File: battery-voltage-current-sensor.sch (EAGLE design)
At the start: 1 part

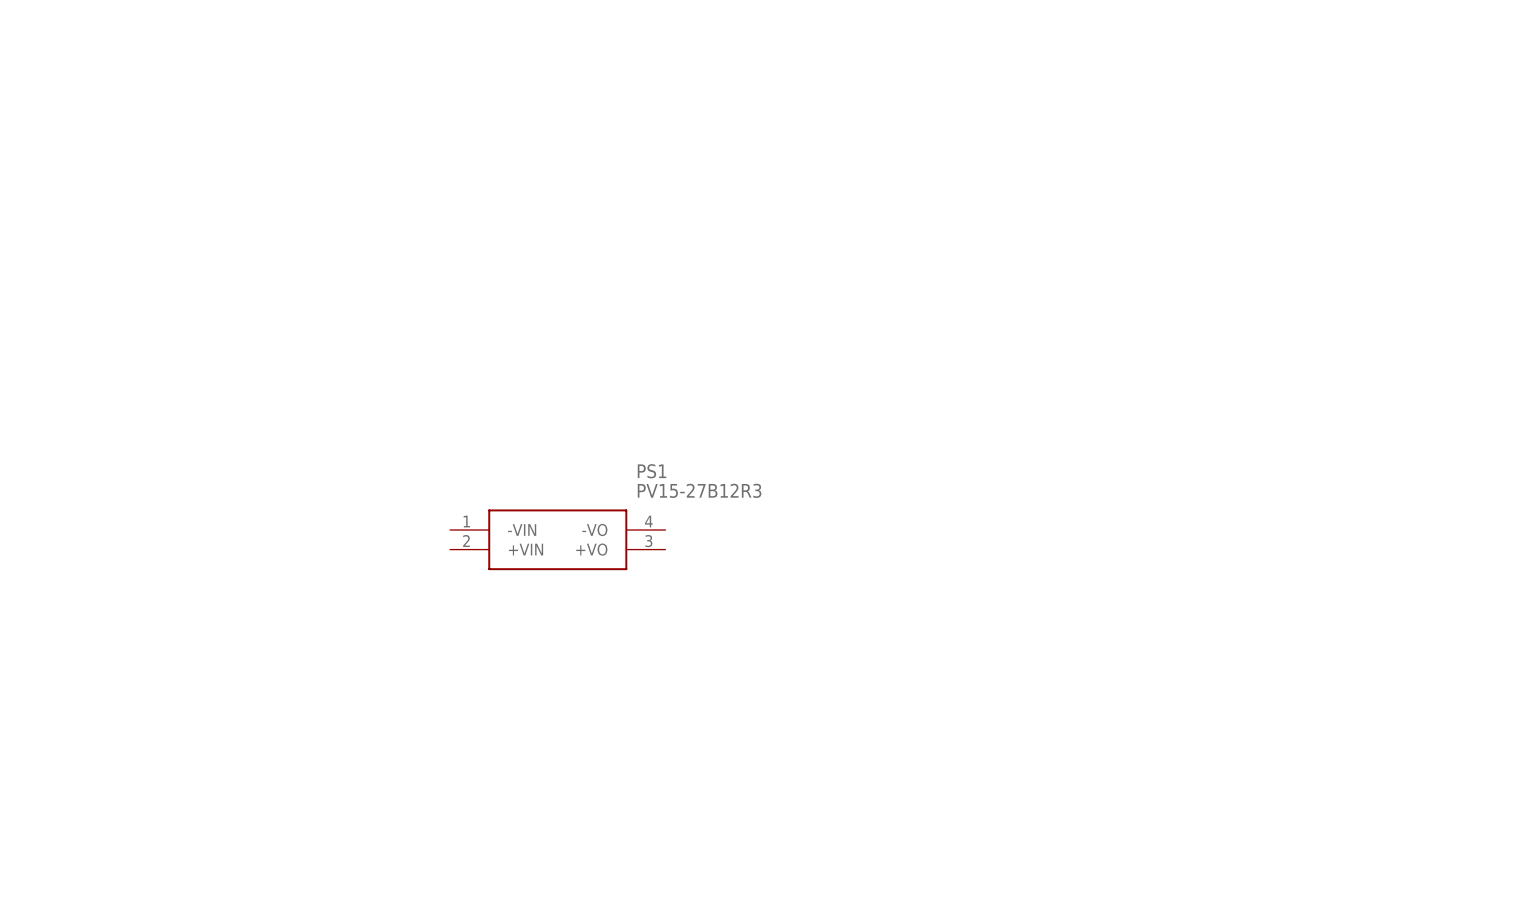
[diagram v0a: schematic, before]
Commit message: basic board and holes added
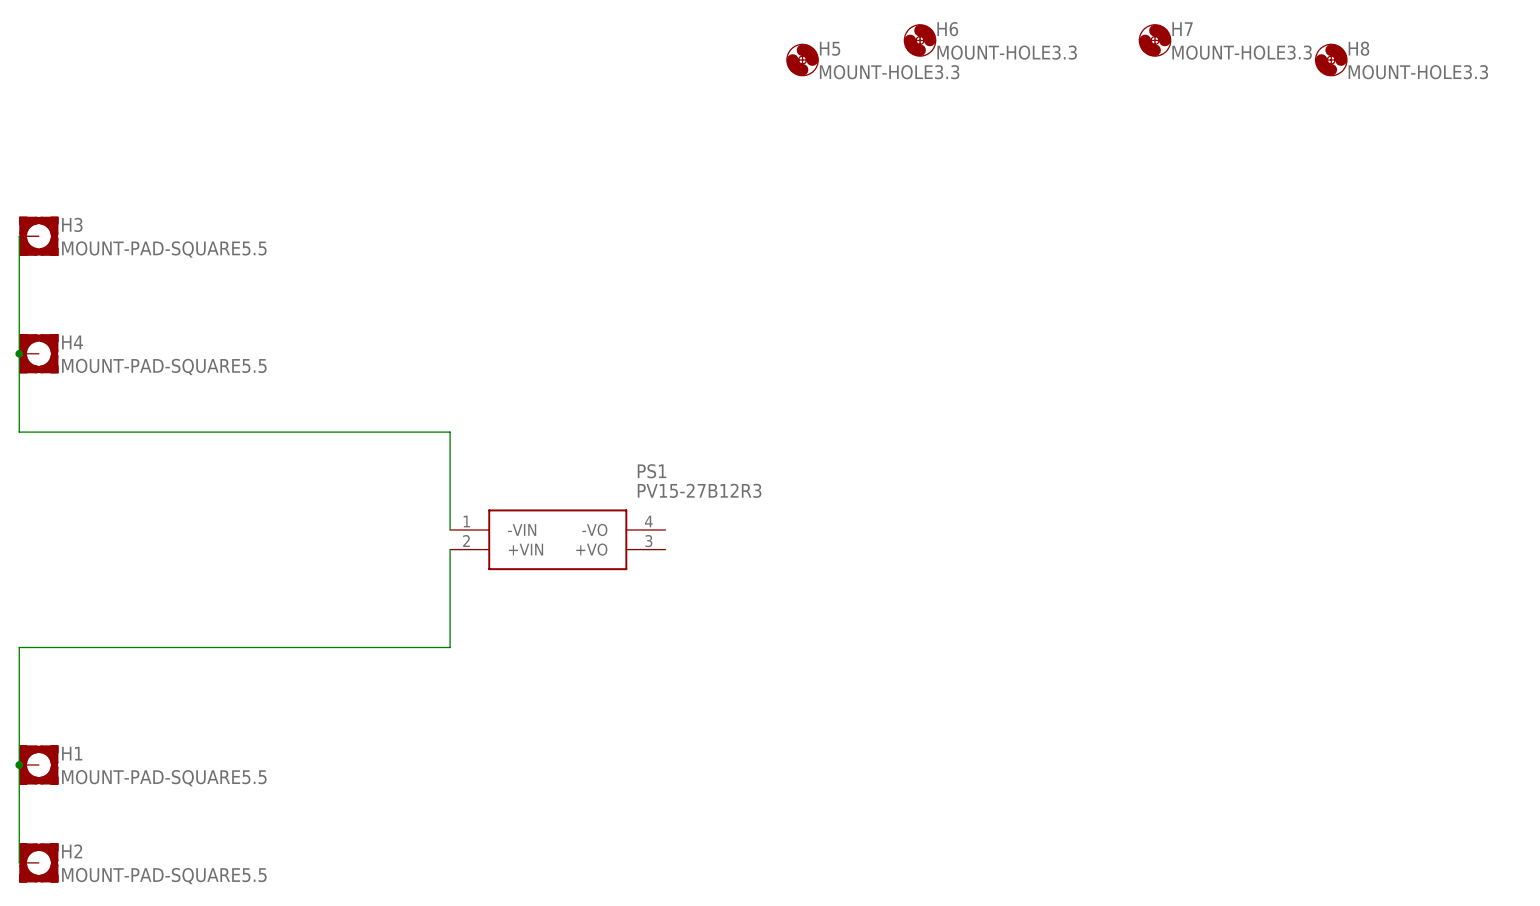
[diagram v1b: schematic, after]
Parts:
- added H1, H2, H3, H4: MOUNT-PAD-SQUARE5.5, holes:MOUNT-PAD-SQUARE5.5
- added H5, H6, H7, H8: MOUNT-HOLE3.3, holes:MOUNT-HOLE3.3
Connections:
- new net N$1: H1.MOUNT, H2.MOUNT, PS1.+VIN
- new net N$2: H3.MOUNT, H4.MOUNT, PS1.-VIN
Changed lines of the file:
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@@
 <parts>
 <part name="PS1" library="SamacSys_Parts" deviceset="PV15-27B12R3" device=""/>
+<part name="H1" library="holes" library_urn="urn:adsk.eagle:library:237" deviceset="MOUNT-PAD-SQUARE" device="5.5" package3d_urn="urn:adsk.eagle:package:14299/1"/>
+<part name="H2" library="holes" library_urn="urn:adsk.eagle:library:237" deviceset="MOUNT-PAD-SQUARE" device="5.5" package3d_urn="urn:adsk.eagle:package:14299/1"/>
+<part name="H3" library="holes" library_urn="urn:adsk.eagle:library:237" deviceset="MOUNT-PAD-SQUARE" device="5.5" package3d_urn="urn:adsk.eagle:package:14299/1"/>
+<part name="H4" library="holes" library_urn="urn:adsk.eagle:library:237" deviceset="MOUNT-PAD-SQUARE" device="5.5" package3d_urn="urn:adsk.eagle:package:14299/1"/>
+<part name="H5" library="holes" library_urn="urn:adsk.eagle:library:237" deviceset="MOUNT-HOLE" device="3.3" package3d_urn="urn:adsk.eagle:package:14278/1"/>
+<part name="H6" library="holes" library_urn="urn:adsk.eagle:library:237" deviceset="MOUNT-HOLE" device="3.3" package3d_urn="urn:adsk.eagle:package:14278/1"/>
+<part name="H7" library="holes" library_urn="urn:adsk.eagle:library:237" deviceset="MOUNT-HOLE" device="3.3" package3d_urn="urn:adsk.eagle:package:14278/1"/>
+<part name="H8" library="holes" library_urn="urn:adsk.eagle:library:237" deviceset="MOUNT-HOLE" device="3.3" package3d_urn="urn:adsk.eagle:package:14278/1"/>
 </parts>
 <sheets>
@@
 <attribute name="VALUE" x="77.47" y="68.58" size="1.778" layer="96" align="center-left"/>
 </instance>
+<instance part="H1" gate="G$1" x="0" y="33.02" smashed="yes">
+<attribute name="NAME" x="2.794" y="33.6042" size="1.778" layer="95"/>
+<attribute name="VALUE" x="2.794" y="30.5562" size="1.778" layer="96"/>
+</instance>
+<instance part="H2" gate="G$1" x="0" y="20.32" smashed="yes">
+<attribute name="NAME" x="2.794" y="20.9042" size="1.778" layer="95"/>
+<attribute name="VALUE" x="2.794" y="17.8562" size="1.778" layer="96"/>
+</instance>
+<instance part="H3" gate="G$1" x="0" y="101.6" smashed="yes">
+<attribute name="NAME" x="2.794" y="102.1842" size="1.778" layer="95"/>
+<attribute name="VALUE" x="2.794" y="99.1362" size="1.778" layer="96"/>
+</instance>
+<instance part="H4" gate="G$1" x="0" y="86.36" smashed="yes">
+<attribute name="NAME" x="2.794" y="86.9442" size="1.778" layer="95"/>
+<attribute name="VALUE" x="2.794" y="83.8962" size="1.778" layer="96"/>
+</instance>
+<instance part="H5" gate="G$1" x="99.06" y="124.46" smashed="yes">
+<attribute name="NAME" x="101.092" y="125.0442" size="1.778" layer="95"/>
+<attribute name="VALUE" x="101.092" y="121.9962" size="1.778" layer="96"/>
+</instance>
+<instance part="H6" gate="G$1" x="114.3" y="127" smashed="yes">
+<attribute name="NAME" x="116.332" y="127.5842" size="1.778" layer="95"/>
+<attribute name="VALUE" x="116.332" y="124.5362" size="1.778" layer="96"/>
+</instance>
+<instance part="H7" gate="G$1" x="144.78" y="127" smashed="yes">
+<attribute name="NAME" x="146.812" y="127.5842" size="1.778" layer="95"/>
+<attribute name="VALUE" x="146.812" y="124.5362" size="1.778" layer="96"/>
+</instance>
+<instance part="H8" gate="G$1" x="167.64" y="124.46" smashed="yes">
+<attribute name="NAME" x="169.672" y="125.0442" size="1.778" layer="95"/>
+<attribute name="VALUE" x="169.672" y="121.9962" size="1.778" layer="96"/>
+</instance>
 </instances>
 <busses>
 </busses>
 <nets>
+<net name="N$1" class="0">
+<segment>
+<pinref part="H1" gate="G$1" pin="MOUNT"/>
+<pinref part="H2" gate="G$1" pin="MOUNT"/>
+<wire x1="-2.54" y1="33.02" x2="-2.54" y2="20.32" width="0.1524" layer="91"/>
+<pinref part="PS1" gate="G$1" pin="+VIN"/>
+<wire x1="53.34" y1="60.96" x2="53.34" y2="48.26" width="0.1524" layer="91"/>
+<wire x1="53.34" y1="48.26" x2="-2.54" y2="48.26" width="0.1524" layer="91"/>
+<wire x1="-2.54" y1="48.26" x2="-2.54" y2="33.02" width="0.1524" layer="91"/>
+<junction x="-2.54" y="33.02"/>
+</segment>
+</net>
+<net name="N$2" class="0">
+<segment>
+<pinref part="H4" gate="G$1" pin="MOUNT"/>
+<pinref part="H3" gate="G$1" pin="MOUNT"/>
+<wire x1="-2.54" y1="86.36" x2="-2.54" y2="101.6" width="0.1524" layer="91"/>
+<wire x1="-2.54" y1="86.36" x2="-2.54" y2="76.2" width="0.1524" layer="91"/>
+<wire x1="-2.54" y1="76.2" x2="53.34" y2="76.2" width="0.1524" layer="91"/>
+<junction x="-2.54" y="86.36"/>
+<pinref part="PS1" gate="G$1" pin="-VIN"/>
+<wire x1="53.34" y1="76.2" x2="53.34" y2="63.5" width="0.1524" layer="91"/>
+</segment>
+</net>
 </nets>
 </sheet>
@@
 </schematic>
 </drawing>
+<compatibility>
+<note version="8.2" severity="warning">
+Since Version 8.2, EAGLE supports online libraries. The ids
+of those online libraries will not be understood (or retained)
+with this version.
+</note>
+<note version="8.3" severity="warning">
+Since Version 8.3, EAGLE supports URNs for individual library
+assets (packages, symbols, and devices). The URNs of those assets
+will not be understood (or retained) with this version.
+</note>
+<note version="8.3" severity="warning">
+Since Version 8.3, EAGLE supports the association of 3D packages
+with devices in libraries, schematics, and board files. Those 3D
+packages will not be understood (or retained) with this version.
+</note>
+</compatibility>
 </eagle>

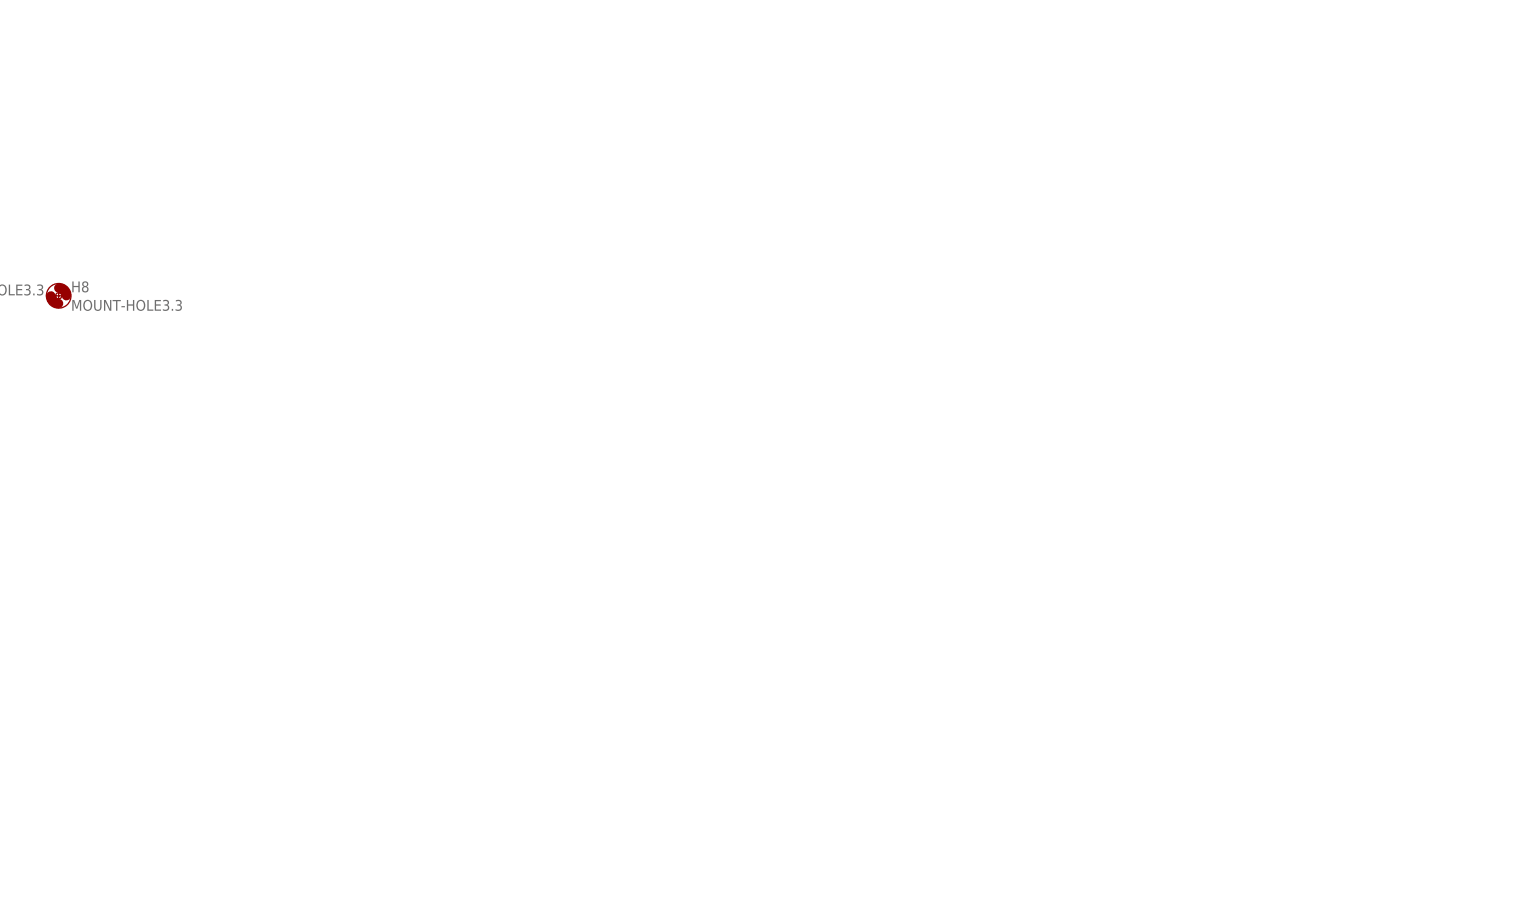
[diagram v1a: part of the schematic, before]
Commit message: mounting holes added
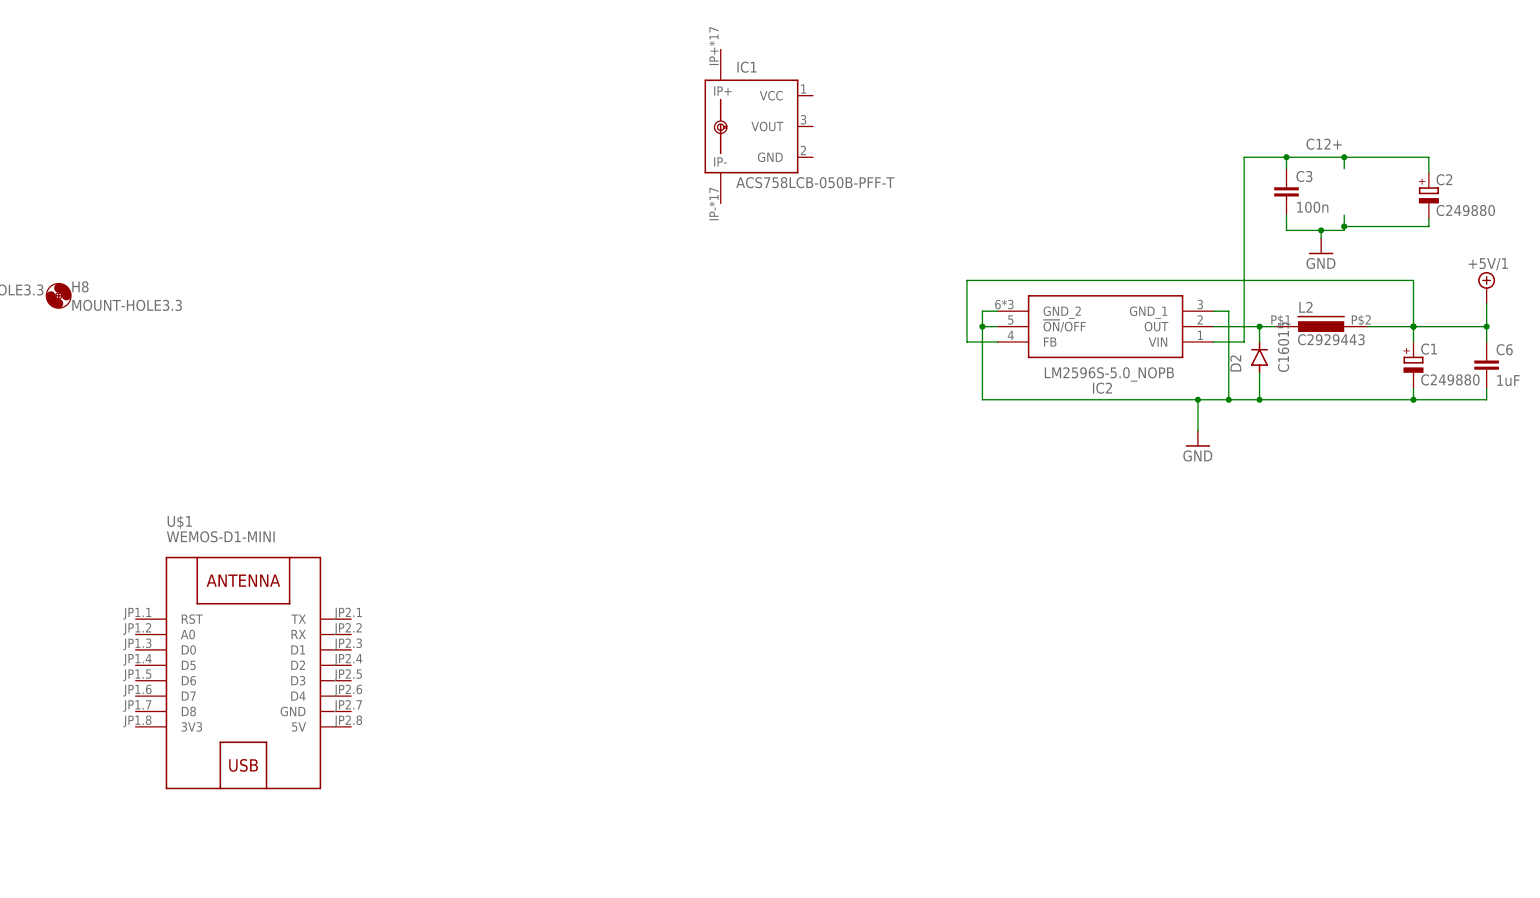
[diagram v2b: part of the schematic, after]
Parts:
- added C1, C2: C249880, rcl:CPOL-EUUD-8X10
- added C3: 100n, rcl:C-EUC0402
- added C6: 1uF, rcl:C-EUC1206
- added D2: C16015, diode:DIODE-DO214AC
- added IC1: ACS758LCB-050B-PFF-T, allegro:ACS758LCB-050B-PFF-T
- added IC2: LM2596S-5.0_NOPB, SamacSys_Parts:LM2596S-5.0_NOPB
- added L2: C2929443, SamacSys_Parts:CY75-100UH
- added U$1: WEMOS-D1-MINI, diy-modules:WEMOS-D1-MINI
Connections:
- new net +5V/1: C1.+, C6.1, IC2.FB, L2.2
- new net C12+: C2.+, C3.1, IC2.VIN
- new net GND: C1.-, C2.-, C3.2, C6.2, D2.A, IC2.!ON!/OFF, IC2.GND_1, IC2.GND_2
- new net N$3: D2.C, IC2.OUT, L2.1

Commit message: DCDC as a module added
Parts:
- removed D2: C16015, diode:DIODE-DO214AC
- removed IC2: LM2596S-5.0_NOPB, SamacSys_Parts:LM2596S-5.0_NOPB
- removed L2: C2929443, SamacSys_Parts:CY75-100UH
- added C10, C11, C12, C13, C14, C15, C5, C7, C8, C9: 100nF, rcl:C-EUC0603
- added C4: 100nF, rcl:C-EUC0805
- added IC3: ADS1115IDGST, SamacSys_Parts:ADS1115IDGST
- added R1, R2, R3: 10k, rcl:R-EU_R0603
- added R15, R16, R17, R18, R19, R20, R21, R22, R23, R4: 120k, rcl:R-EU_R1206
- added R24: 10k 1206, rcl:R-EU_R1206
- added R5, R6, R7, R8: 1k, rcl:R-EU_R0805
- added U$2: DC-DC-STEP-DOWN-LM2596HVS, diy-modules:DC-DC-STEP-DOWN-LM2596HVS
- C1: value C249880 -> C473426; device rcl:CPOL-EUUD-8X10 -> rcl:CPOL-EUUD-6,3X7,7
- C2: value C249880 -> (none); device rcl:CPOL-EUUD-8X10 -> rcl:CPOL-EUUD-6,3X7,7
- C3: value 100n -> 100nF; device rcl:C-EUC0402 -> rcl:C-EUC0603
- C6: value 1uF -> 100nF; device rcl:C-EUC1206 -> rcl:C-EUC0603
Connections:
- removed net C12+: C2.+, C3.1, IC2.VIN
- removed net N$2: H3.MOUNT, H4.MOUNT, PS1.-VIN
- new net +12V/1: C1.+, C3.1, C5.1, PS1.+VO, U$2.IN+
- new net +3.3V/1: R1.2, R2.2, R3.2, U$1.3V3
- new net AIN0: C13.1, IC3.AIN0, R8.1
- new net AIN1: C12.1, IC3.AIN1, R7.1
- new net AIN2: C11.1, IC3.AIN2, R6.1
- new net AIN3: C10.1, IC3.AIN3, R5.1
- new net HV+: H1.MOUNT, H2.MOUNT, PS1.+VIN, R23.2
- new net HV-: H4.MOUNT, IC1.IP-, PS1.-VIN, R24.1
- new net HV-IN: H3.MOUNT, IC1.IP+
- new net N$10: R16.2, R17.1
- new net N$11: R17.2, R18.1
- new net N$12: R18.2, R19.1
- new net N$13: R19.2, R20.1
- new net N$14: R20.2, R21.1
- new net N$15: R21.2, R22.1
- new net N$16: R22.2, R23.1
- new net N$18: R7.2
- new net N$4: IC3.SCL, R2.1, U$1.D1
- new net N$5: IC3.SDA, R3.1, U$1.D2
- new net N$7: R6.2
- new net N$8: R15.1, R4.2
- new net N$9: R15.2, R16.1
- new net SIGNALHV: R24.2, R4.1
- new net VOUTCURRENT: IC1.VOUT, R8.2
- net +5V/1: now also C14.1, C15.1, C2.+, C4.1, C7.1, C8.2, C9.2, IC1.VCC, IC3.VDD, U$1.5V, U$2.OUT+; no longer C1.+, IC2.FB, L2.2
- net GND: now also C10.2, C11.2, C12.2, C13.2, C14.2, C15.2, C4.2, C5.2, C7.2, C8.1, C9.1, IC1.GND, IC3.ADDR, IC3.GND, PS1.-VO, U$1.GND, U$2.IN-, U$2.OUT-; no longer D2.A, IC2.!ON!/OFF, IC2.GND_1, IC2.GND_2
- net N$1: now also IC3.ALERT/RDY, R1.1, U$1.D3; no longer H1.MOUNT, H2.MOUNT, PS1.+VIN
- net N$3: now also R5.2; no longer D2.C, IC2.OUT, L2.1
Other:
- note added: "HV+In"
- note added: "HV+Out"
- note added: "HV-Out"
- moved on the sheet: C1, C2, C3, C6, H2, H3, H4, H5, H6, H7, H8, IC1

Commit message: first placing succes
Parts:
- added D1: C78395, diode:DIODE-SMB
- added D3, D4, D5, D6: KT-0603R, SMD-LED-CLEAR-BLUE_0603_:SMD-LED-CLEAR-BLUE(0603)
- added R10, R12: C13564, rcl:R-EU_R0603
- added R11, R9: 10k, rcl:R-EU_R0603
- added R14, R25, R26, R27: 1k, rcl:R-EU_R0805
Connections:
- removed net SIGNALHV: R24.2, R4.1
- new net N$17: D6.+, R27.1
- new net N$19: R14.2, U$1.D7
- new net N$20: R25.2, U$1.D6
- new net N$21: R26.2, U$1.D5
- new net N$6: D4.+, R25.1
- new net VOUTHV: R24.2, R4.1, R8.2
- new net VOUTNTC1: R10.2, R6.2, R9.1
- new net VOUTNTC2: R11.1, R12.2, R5.2
- net +5V/1: now also D1.C, R11.2, R9.2
- net GND: now also D1.A, D3.-, D4.-, D5.-, D6.-, R10.1, R12.1
- net HV-: no longer R24.1
- net HV-IN: now also R24.1
- net N$18: now also R27.2, U$1.D8; no longer R7.2
- net N$3: now also D3.+, R14.1; no longer R5.2
- net N$7: now also D5.+, R26.1; no longer R6.2
- net VOUTCURRENT: now also R7.2; no longer R8.2
